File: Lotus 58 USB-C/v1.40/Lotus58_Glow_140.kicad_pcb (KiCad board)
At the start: 2 copper layers, 139.1 x 107.7 mm, 121 parts, among them J3 USB_C_Receptacle_USB2.0, P1 OLED, SW1 Kailh hotswap Choc V1 socket, SW10 Kailh hotswap Choc V1 socket, SW11 Kailh hotswap Choc V1 socket, SW12 Kailh hotswap Choc V1 socket, SW13 Kailh hotswap Choc V1 socket, SW14 Kailh hotswap Choc V1 socket, SW15 Kailh hotswap Choc V1 socket, SW16 Kailh hotswap Choc V1 socket, SW17 Kailh hotswap Choc V1 socket, SW18 Kailh hotswap Choc V1 socket, SW19 Kailh hotswap Choc V1 socket, SW2 Kailh hotswap Choc V1 socket, SW20 Kailh hotswap Choc V1 socket, SW21 Kailh hotswap Choc V1 socket, SW22 Kailh hotswap Choc V1 socket, SW23 Kailh hotswap Choc V1 socket, SW24 Kailh hotswap Choc V1 socket, SW25 Kailh hotswap Choc V1 socket, SW26 Kailh hotswap Choc V1 socket, SW27 Kailh hotswap Choc V1 socket, SW28 Kailh hotswap Choc V1 socket, SW29 Kailh hotswap Choc V1 socket, SW3 Kailh hotswap Choc V1 socket, SW30 Rotary_Encoder_Switch, SW32 MSK12C02, SW33 MSK12C02, SW4 Kailh hotswap Choc V1 socket, SW5 Kailh hotswap Choc V1 socket, SW6 Kailh hotswap Choc V1 socket, SW7 Kailh hotswap Choc V1 socket, SW8 Kailh hotswap Choc V1 socket, SW9 Kailh hotswap Choc V1 socket, U1 ProMicro, U2 SRV05-4, U3 SRV05-4, U4 SN74LVC1T45DBVR, U5 SN74LVC1T45DBVR

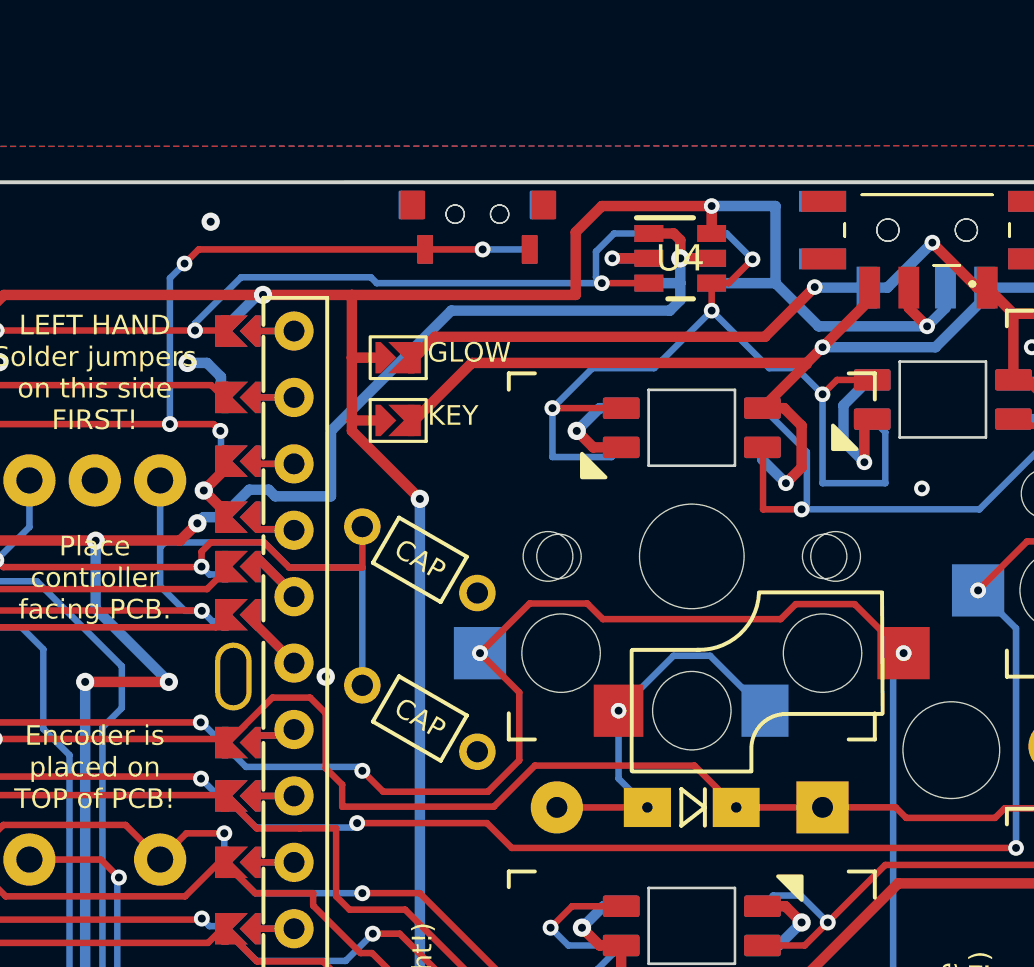
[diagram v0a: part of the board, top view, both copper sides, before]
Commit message: Added decoupling capacitors for level shifter
* Also changed encoder decoupling capacitors to SMD components
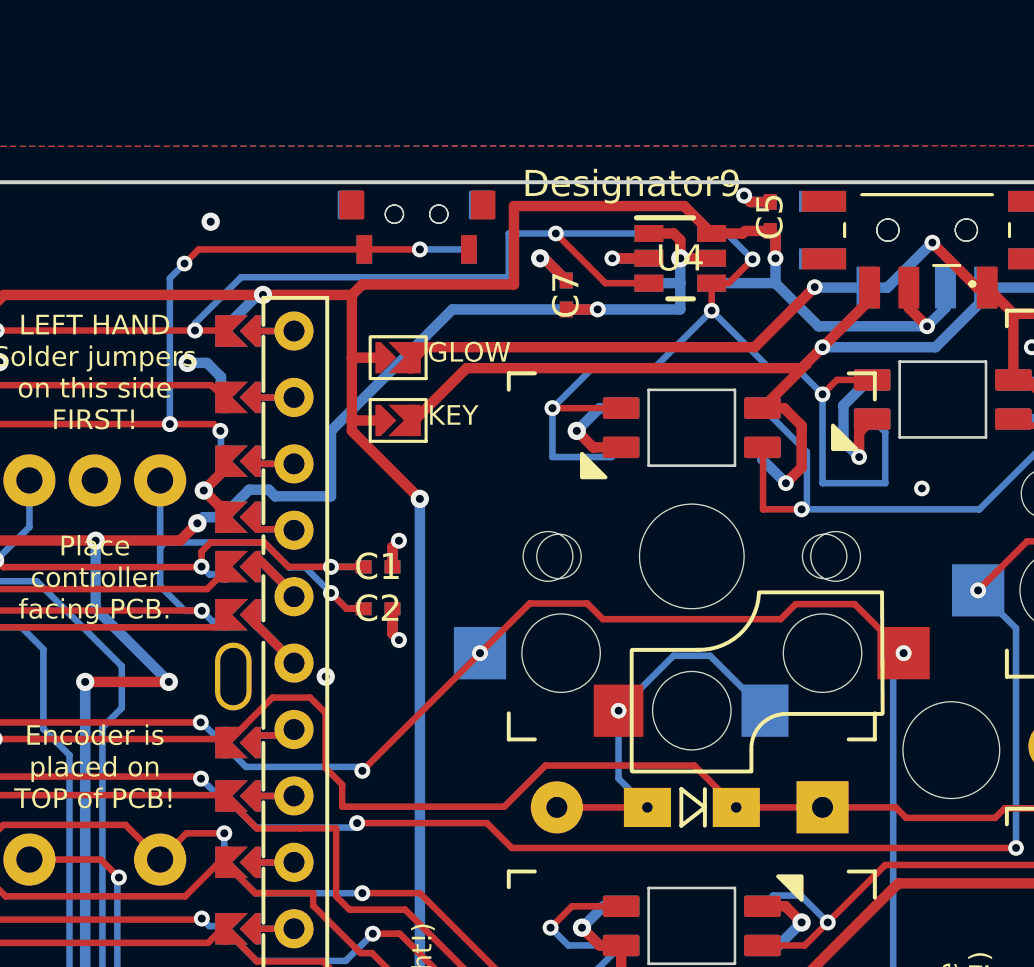
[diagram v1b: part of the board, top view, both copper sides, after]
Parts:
- added C3: 100nF, Spencer-Custom:CAP_CL05_SAM, B.Cu at (102.4, 52.0)
- added C4: 100nF, Spencer-Custom:CAP_CL05_SAM, B.Cu at (102.4, 50.4)
- added C5: 100nF, Spencer-Custom:CAP_CL05_SAM, F.Cu at (117.4, 37.0)
- added C6: 100nF, Spencer-Custom:CAP_CL05_SAM, B.Cu at (117.4, 37.0)
- added C7: 100nF, Spencer-Custom:CAP_CL05_SAM, F.Cu at (109.6, 40.0)
- added C8: 100nF, Spencer-Custom:CAP_CL05_SAM, B.Cu at (109.6, 40.0)
- C1, C2: footprint Keyboard Common:RESISTOR_Reversible -> Spencer-Custom:CAP_CL05_SAM; moved to F.Cu
- moved C2 4.49 mm to (102.4, 52.0), turned to 0 degrees
- moved RES1 2.33 mm to (103.9, 36.9)
- moved RES2 2.33 mm to (103.9, 36.9)
- moved C1 1.62 mm to (102.4, 50.4), turned to 0 degrees
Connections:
- C2 pad 1: GND -> EncA
- C2 pad 2: EncA -> GND
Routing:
- net GND: track 171.6 -> 180.9 mm, vias 90 -> 94
- net col5: track 197.5 -> 192.3 mm
- net VCC: track 83.8 -> 87.6 mm, vias 7 -> 8
- net RESET: track 31.9 -> 29.6 mm
- net LED: track 31.8 -> 34.1 mm
- net EncA: track 28.7 -> 26.4 mm, vias 1 -> 2
- net EncB: track 22.5 -> 22.2 mm, vias 2 -> 3

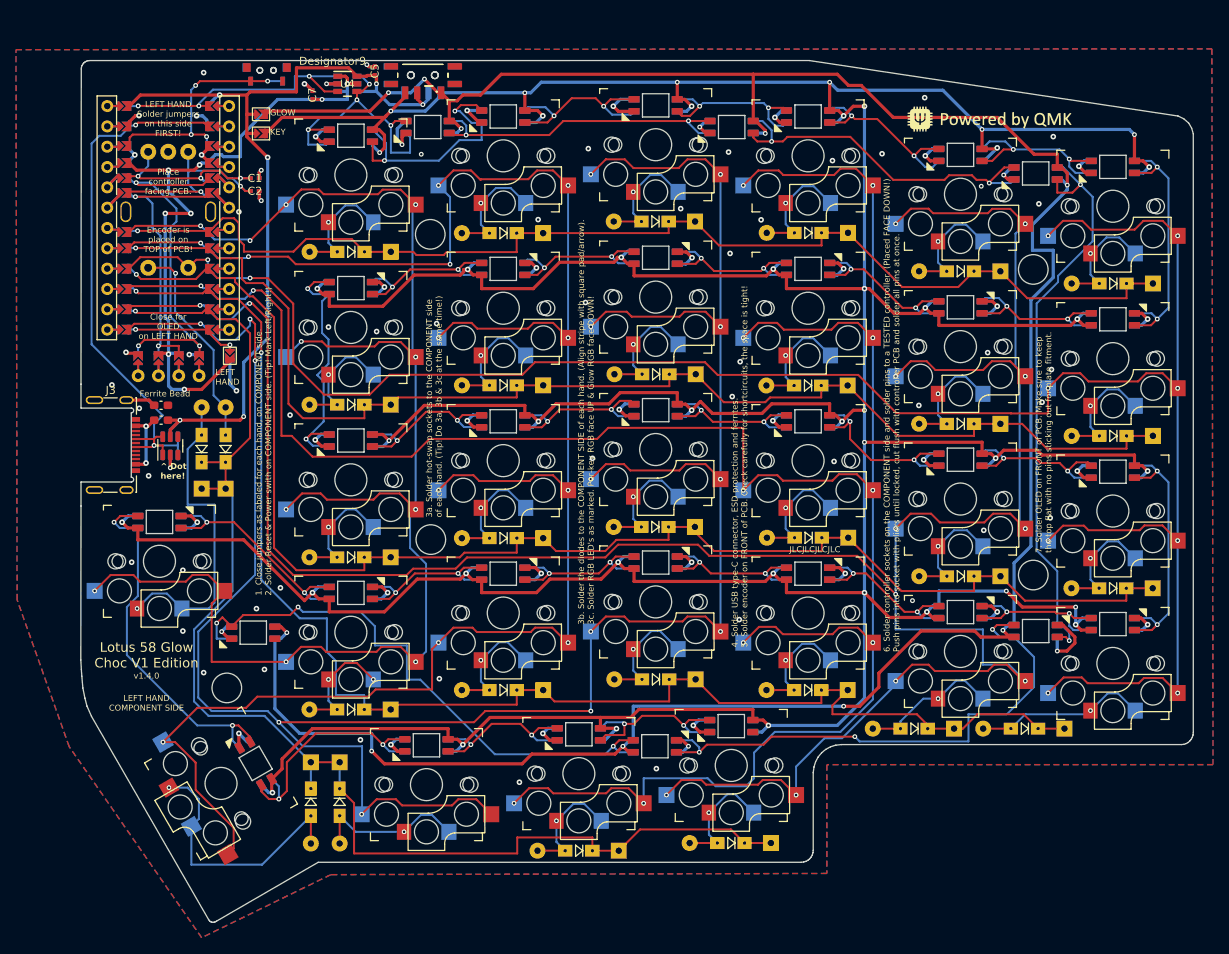
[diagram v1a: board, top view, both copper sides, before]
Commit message: Small trace changes to appease JLCDFM
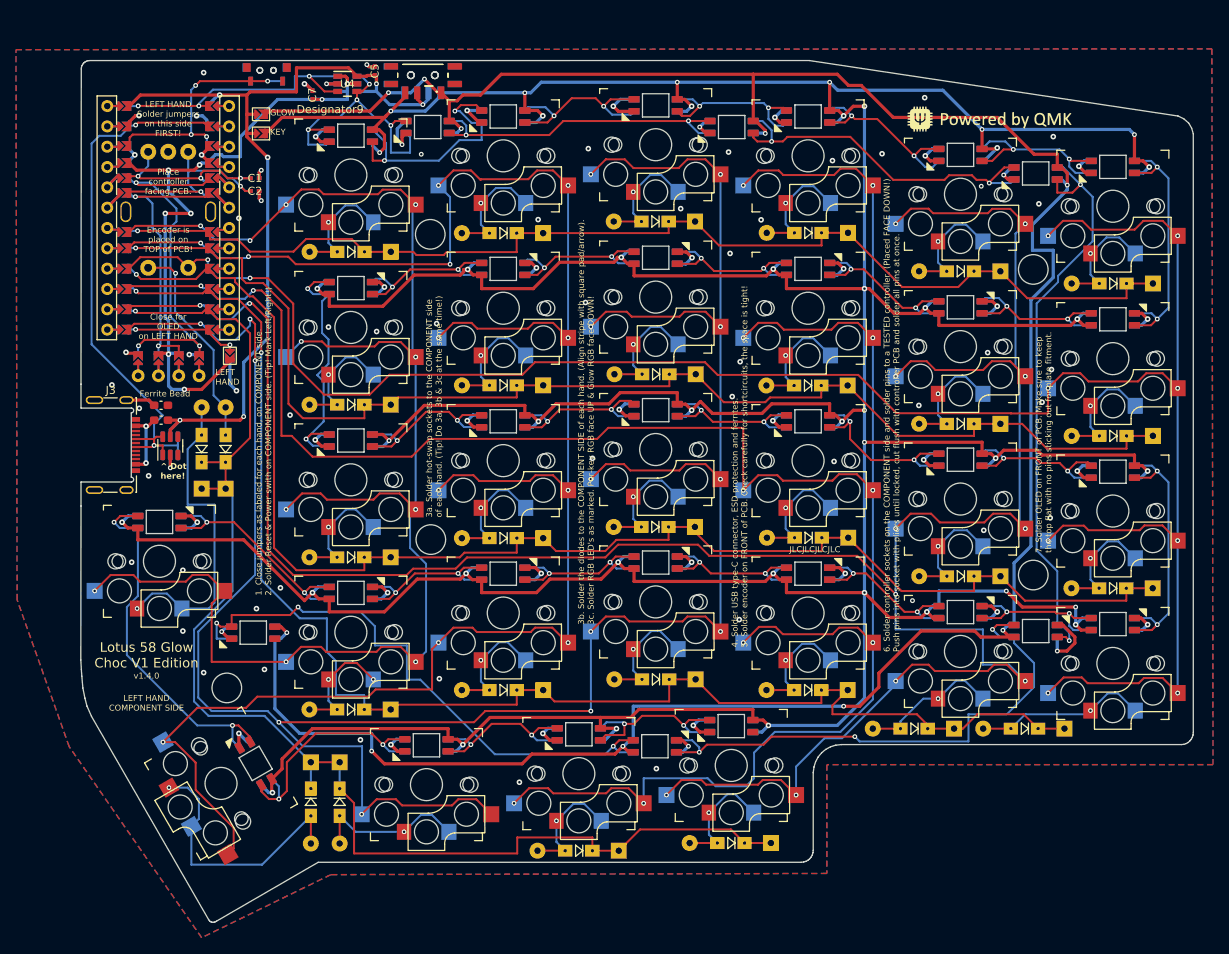
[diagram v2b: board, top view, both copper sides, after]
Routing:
- net row0: track 147.2 -> 144.8 mm
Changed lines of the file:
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@@
 		(aux_axis_origin 76.0603 36.6903)
 		(pcbplotparams
-			(layerselection 0x00010f0_ffffffff)
+			(layerselection 0x00010fc_ffffffff)
 			(plot_on_all_layers_selection 0x0000000_00000000)
 			(disableapertmacros no)
 			(usegerberextensions yes)
-			(usegerberattributes yes)
+			(usegerberattributes no)
 			(usegerberadvancedattributes no)
 			(creategerberjobfile no)
@@
 		)
 		(fp_text user "Designator9"
-			(at -1.8542 -2.8448 0)
+			(at -2.160051 3.2 0)
 			(unlocked yes)
 			(layer "F.SilkS")
@@
 		(fp_arc
 			(start -0.576537 0.906071)
-			(mid -0.449563 0.779098)
+			(mid -0.449563 0.779101)
 			(end -0.322588 0.906071)
 			(stroke
@@
 	)
 	(segment
-		(start 101.0298 58.7298)
-		(end 101.0298 59.5702)
-		(width 0.25)
-		(layer "F.Cu")
-		(net 5)
-	)
-	(segment
 		(start 176.53746 57.23)
 		(end 176.54 57.22746)
@@
 	)
 	(segment
-		(start 135.14 57.26)
-		(end 135.14254 57.25746)
+		(start 107.2298 59.5702)
+		(end 108.8 58)
 		(width 0.25)
 		(layer "F.Cu")
@@
 	)
 	(segment
-		(start 192.29 62.03)
-		(end 195.58746 62.03)
+		(start 135.14 57.26)
+		(end 135.14254 57.25746)
 		(width 0.25)
 		(layer "F.Cu")
@@
 	)
 	(segment
-		(start 96.779 56.983308)
-		(end 98.362308 55.4)
+		(start 192.29 62.03)
+		(end 195.58746 62.03)
 		(width 0.25)
 		(layer "F.Cu")
@@
 	)
 	(segment
-		(start 154.12 57.25746)
-		(end 154.12 55.81)
+		(start 101.7702 59.5702)
+		(end 107.2298 59.5702)
 		(width 0.25)
 		(layer "F.Cu")
@@
 	)
 	(segment
-		(start 99.8 55.4)
-		(end 100.4 56)
+		(start 154.12 57.25746)
+		(end 154.12 55.81)
 		(width 0.25)
 		(layer "F.Cu")
@@
 	)
 	(segment
-		(start 100.4 56)
-		(end 100.4 58.1)
-		(width 0.25)
-		(layer "F.Cu")
-		(net 5)
-	)
-	(segment
 		(start 135.14254 57.25746)
 		(end 138.43 57.25746)
@@
 	)
 	(segment
-		(start 211.36 63.56)
-		(end 211.56 63.56)
+		(start 96.779 58.05)
+		(end 100.25 58.05)
 		(width 0.25)
 		(layer "F.Cu")
@@
 	)
 	(segment
-		(start 122.19746 59.59746)
-		(end 119.4 59.59746)
+		(start 211.36 63.56)
+		(end 211.56 63.56)
 		(width 0.25)
 		(layer "F.Cu")
@@
 	)
 	(segment
-		(start 98.362308 55.4)
-		(end 99.8 55.4)
+		(start 122.19746 59.59746)
+		(end 119.4 59.59746)
 		(width 0.25)
 		(layer "F.Cu")
@@
 	)
 	(segment
-		(start 107.2298 59.5702)
-		(end 108.8 58)
+		(start 116.1 59.6)
+		(end 119.39746 59.6)
 		(width 0.25)
 		(layer "F.Cu")
@@
 	)
 	(segment
-		(start 116.1 59.6)
-		(end 119.39746 59.6)
+		(start 87.740833 56.980133)
+		(end 87.744008 56.983308)
 		(width 0.25)
 		(layer "F.Cu")
@@
 	)
 	(segment
-		(start 160.41254 58.8)
-		(end 173.24 58.8)
+		(start 100.25 58.05)
+		(end 101.7702 59.5702)
 		(width 0.25)
 		(layer "F.Cu")
@@
 	)
 	(segment
-		(start 108.8 58)
-		(end 114.5 58)
+		(start 87.744008 56.983308)
+		(end 96.779 56.983308)
 		(width 0.25)
 		(layer "F.Cu")
@@
 	)
 	(segment
-		(start 114.5 58)
-		(end 116.1 59.6)
+		(start 160.41254 58.8)
+		(end 173.24 58.8)
 		(width 0.25)
 		(layer "F.Cu")
@@
 	)
 	(segment
-		(start 87.740833 56.980133)
-		(end 87.744008 56.983308)
+		(start 108.8 58)
+		(end 114.5 58)
 		(width 0.25)
 		(layer "F.Cu")
@@
 	)
 	(segment
-		(start 87.744008 56.983308)
-		(end 96.779 56.983308)
+		(start 190.32 64)
+		(end 192.29 62.03)
 		(width 0.25)
 		(layer "F.Cu")
@@
 	)
 	(segment
-		(start 190.32 64)
-		(end 192.29 62.03)
+		(start 96.779 56.983308)
+		(end 96.779 58.05)
+		(width 0.25)
+		(layer "F.Cu")
+		(net 5)
+	)
+	(segment
+		(start 114.5 58)
+		(end 116.1 59.6)
 		(width 0.25)
 		(layer "F.Cu")
@@
 	)
 	(segment
-		(start 101.0298 59.5702)
-		(end 107.2298 59.5702)
-		(width 0.25)
-		(layer "F.Cu")
-		(net 5)
-	)
-	(segment
 		(start 211.36 65.4)
 		(end 211.36 63.56)
@@
 	)
 	(segment
-		(start 100.4 58.1)
-		(end 101.0298 58.7298)
-		(width 0.25)
-		(layer "F.Cu")
-		(net 5)
-	)
-	(segment
 		(start 135.13 57.26)
 		(end 135.14 57.26)
@@
 	)
 	(via
-		(at 100.4 54.6)
+		(at 100.4 55.4)
 		(size 0.7)
 		(drill 0.3048)
@@
 	)
 	(segment
+		(start 199.8 114)
+		(end 199.8 111)
+		(width 0.25)
+		(layer "B.Cu")
+		(net 90)
+	)
+	(segment
 		(start 157.95 122.15)
 		(end 157.95 121.55)
@@
 	)
 	(segment
-		(start 191.6 117.4)
-		(end 196.4 117.4)
+		(start 199.8 111)
+		(end 197.3 108.5)
 		(width 0.25)
 		(layer "B.Cu")
@@
 	)
 	(segment
-		(start 177.4 120.2)
-		(end 178 120.8)
+		(start 178 120.8)
+		(end 191.6 120.8)
 		(width 0.25)
 		(layer "B.Cu")
@@
 	)
 	(segment
-		(start 191.6 120.8)
-		(end 191.6 117.4)
+		(start 191.6 117.4)
+		(end 196.4 117.4)
 		(width 0.25)
 		(layer "B.Cu")
@@
 	)
 	(segment
-		(start 199.8 110.25)
-		(end 197.3 107.75)
+		(start 177.4 120.2)
+		(end 178 120.8)
 		(width 0.25)
 		(layer "B.Cu")
@@
 	)
 	(segment
-		(start 157.95 121.55)
-		(end 157.050002 120.650002)
+		(start 197.3 108.5)
+		(end 197.3 107.75)
 		(width 0.25)
 		(layer "B.Cu")
@@
 	)
 	(segment
-		(start 199.8 114)
-		(end 199.8 110.25)
+		(start 157.95 121.55)
+		(end 157.050002 120.650002)
 		(width 0.25)
 		(layer "B.Cu")
@@
 	)
 	(segment
-		(start 194.6 106.8)
-		(end 195.55 107.75)
+		(start 196.4 117.4)
+		(end 199.8 114)
 		(width 0.25)
 		(layer "B.Cu")
@@
 	)
 	(segment
-		(start 195.55 107.75)
-		(end 197.3 107.75)
+		(start 194.6 106.8)
+		(end 195.55 107.75)
 		(width 0.25)
 		(layer "B.Cu")
@@
 	)
 	(segment
-		(start 157.050002 120.650002)
-		(end 155.1 120.650002)
+		(start 191.6 120.8)
+		(end 191.6 117.4)
 		(width 0.25)
 		(layer "B.Cu")
@@
 	)
 	(segment
-		(start 196.4 117.4)
-		(end 199.8 114)
+		(start 195.55 107.75)
+		(end 197.3 107.75)
 		(width 0.25)
 		(layer "B.Cu")
@@
 	)
 	(segment
-		(start 178 120.8)
-		(end 191.6 120.8)
+		(start 157.050002 120.650002)
+		(end 155.1 120.650002)
 		(width 0.25)
 		(layer "B.Cu")
@@
 	)
 	(segment
-		(start 147.95 120.65)
-		(end 147.2 121.4)
+		(start 107.8 104)
+		(end 106.8 105)
 		(width 0.25)
 		(layer "F.Cu")
@@
 	)
 	(segment
-		(start 106.8 105)
-		(end 100.95 105)
+		(start 147.95 120.65)
+		(end 147.2 121.4)
 		(width 0.25)
 		(layer "F.Cu")
@@
 	)
 	(segment
-		(start 100.95 105)
-		(end 99.5 106.45)
+		(start 99.5 106.45)
+		(end 98.075 106.45)
 		(width 0.25)
 		(layer "F.Cu")
@@
 	)
 	(segment
-		(start 107.8 104)
-		(end 106.8 105)
+		(start 98.075 106.45)
+		(end 97.625 106)
 		(width 0.25)
 		(layer "F.Cu")
@@
 	)
 	(segment
-		(start 149.7 120.65)
-		(end 147.95 120.65)
+		(start 99.5 105)
+		(end 99.5 106.45)
 		(width 0.25)
 		(layer "F.Cu")
@@
 	)
 	(segment
-		(start 99.5 106.45)
-		(end 98.3375 105.2875)
+		(start 106.8 105)
+		(end 99.5 105)
 		(width 0.25)
 		(layer "F.Cu")
@@
 	)
 	(segment
-		(start 98.3375 105.2875)
-		(end 97.625 106)
+		(start 149.7 120.65)
+		(end 147.95 120.65)
 		(width 0.25)
 		(layer "F.Cu")
